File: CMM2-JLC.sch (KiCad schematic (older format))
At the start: 111 parts, among them J1 Nunchuck, J2 VGA, J3 EXTERNAL I/O, J4 USB_C_Receptacle_USB2.0, J5 Audio, J6 USB A Host, J7 SWD, J8 Micro_SD_Card_Det, J9 Boot select, SW1 Reset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

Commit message: Rev B: Hook up SDRAM address line A12
The old sdram symbol did not fit the sdram used. This commit introduces a
new sdram symbol with address line A12 and bumps the revision to Rev B.
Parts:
- U2: symbol Memory_RAM:AS4C4M16SA -> SDRAM_Micron:MT48LC16M16A2
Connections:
- net PG2: now also U2.36 (A12)
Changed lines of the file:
@@
 Title "Colour Maximite 2"
 Date "2020-07-05"
-Rev "A"
+Rev "B"
 Comp "tbspace.de"
 Comment1 "Tobias Mädel"
@@
 $EndDescr
 $Comp
-L Memory_RAM:AS4C4M16SA U2
+L SDRAM_Micron:MT48LC16M16A2 U2
 U 1 1 5F01B402
 P 6600 9300
@@
 Text Label 5600 9350 0    50   ~ 0
 PG1
-Text Label 5600 9600 0    50   ~ 0
+Text Label 5600 9700 0    50   ~ 0
 PG5
-Text Label 5600 9500 0    50   ~ 0
+Text Label 5600 9600 0    50   ~ 0
 PG4
-Text Label 5600 9750 0    50   ~ 0
-PG8
 Text Label 5600 9850 0    50   ~ 0
+PG8
+Text Label 5600 9950 0    50   ~ 0
 PH7
-Text Label 5600 10000 0    50   ~ 0
+Text Label 5600 10050 0    50   ~ 0
 PF11
-Text Label 5600 10100 0    50   ~ 0
+Text Label 5600 10150 0    50   ~ 0
 PG15
-Text Label 5600 10200 0    50   ~ 0
+Text Label 5600 10250 0    50   ~ 0
 PH5
 Text Label 5600 10350 0    50   ~ 0
@@
 	5800 9350 5600 9350
 Wire Wire Line
-	5600 9600 5800 9600
+	5600 9700 5800 9700
 Wire Wire Line
-	5800 9500 5600 9500
+	5800 9600 5600 9600
 Wire Wire Line
-	5600 9750 5800 9750
+	5600 9850 5800 9850
 Wire Wire Line
-	5800 9850 5600 9850
+	5800 9950 5600 9950
 Wire Wire Line
-	5600 10000 5800 10000
+	5600 10050 5800 10050
 Wire Wire Line
-	5800 10100 5600 10100
+	5800 10150 5600 10150
 Wire Wire Line
-	5800 10200 5600 10200
+	5800 10250 5600 10250
 Wire Wire Line
 	5600 10350 5800 10350
@@
 	11050 8500 11500 8500
 Connection ~ 11050 8500
+Text Label 5600 9450 0    50   ~ 0
+PG2
+Wire Wire Line
+	5800 9450 5600 9450
 $EndSCHEMATC

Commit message: Rev C
Some (mostly cosmetic) changes from the final Rev A gerbers were lost in
Rev B due to a corrupted .kicad_pcb file.

This revision reintroduces those changes and improves overall attachment
of groundplanes and islands to one another. Additionally the VGA connector
footprint has been updated to fit the LCSC connector better.

Changelog:
* Restore changes from Rev A gerbers
* Improve grounding
* Update VGA connector footprint for better fit
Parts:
- J2: footprint Connector_Dsub:DSUB-15-HD_Female_Horizontal_P2.29x1.98mm_EdgePinOffset8.35mm_Housed_MountingHolesOffset10.89mm -> CMM2-JLC:DSUB-15-HD_Female_Horizontal_P2.29x2,54mm_EdgePinOffset8.63mm_Housed_MountingHolesOffset11.17mm; symbol Connector:DB15_Female_HighDensity -> Connector:DB15_Female_HighDensity_MountingHoles
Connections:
- net GND: now also J2.0
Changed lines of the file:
@@
 Title "Colour Maximite 2"
 Date "2020-07-05"
-Rev "B"
+Rev "C"
 Comp "tbspace.de"
 Comment1 "Tobias Mädel"
@@
 	1750 5350 1500 5350
 $Comp
-L Connector:DB15_Female_HighDensity J2
+L Connector:DB15_Female_HighDensity_MountingHoles J2
 U 1 1 5FFE2E3E
-P 14550 5250
-F 0 "J2" H 14550 6117 50  0000 C CNN
-F 1 "VGA" H 14550 6026 50  0000 C CNN
-F 2 "Connector_Dsub:DSUB-15-HD_Female_Horizontal_P2.29x1.98mm_EdgePinOffset8.35mm_Housed_MountingHolesOffset10.89mm" H 13600 5650 50  0001 C CNN
-F 3 " ~" H 13600 5650 50  0001 C CNN
-	1    14550 5250
+P 14550 5100
+F 0 "J2" H 14550 5967 50  0000 C CNN
+F 1 "VGA" H 14550 5876 50  0000 C CNN
+F 2 "CMM2-JLC:DSUB-15-HD_Female_Horizontal_P2.29x2,54mm_EdgePinOffset8.63mm_Housed_MountingHolesOffset11.17mm" H 13600 5500 50  0001 C CNN
+F 3 " ~" H 13600 5500 50  0001 C CNN
+	1    14550 5100
 	1    0    0    -1
 $EndComp
@@
 Wire Wire Line
 	15550 1150 15100 1150
-Text Label 13800 4850 0    50   ~ 0
+Text Label 13800 4700 0    50   ~ 0
 VGA_RED
-Text Label 13800 5050 0    50   ~ 0
+Text Label 13800 4900 0    50   ~ 0
 VGA_GREEN
-Text Label 13800 5250 0    50   ~ 0
+Text Label 13800 5100 0    50   ~ 0
 VGA_BLUE
 Wire Wire Line
-	14250 4850 13800 4850
+	14250 4700 13800 4700
 Wire Wire Line
-	13800 5050 14250 5050
+	13800 4900 14250 4900
 Wire Wire Line
-	14250 5250 13800 5250
-Text Label 15350 5250 2    50   ~ 0
+	14250 5100 13800 5100
+Text Label 15350 5100 2    50   ~ 0
 VGA_HSYNC
-Text Label 15350 5450 2    50   ~ 0
+Text Label 15350 5300 2    50   ~ 0
 VGA_VSYNC
-Text Label 15700 5250 2    50   ~ 0
+Text Label 15700 5100 2    50   ~ 0
 PI10
-Text Label 15700 5450 2    50   ~ 0
+Text Label 15700 5300 2    50   ~ 0
 PI9
 Wire Wire Line
-	14850 5250 15700 5250
+	14850 5100 15700 5100
 Wire Wire Line
-	14850 5450 15700 5450
-NoConn ~ 14850 4850
-NoConn ~ 14850 5050
-NoConn ~ 14850 5650
-NoConn ~ 14250 5450
-NoConn ~ 14250 5350
+	14850 5300 15700 5300
+NoConn ~ 14850 4700
+NoConn ~ 14850 4900
+NoConn ~ 14850 5500
+NoConn ~ 14250 5300
+NoConn ~ 14250 5200
 Wire Wire Line
-	14250 4750 13500 4750
+	14250 4600 13500 4600
 Wire Wire Line
-	14250 4950 13500 4950
+	14250 4800 13500 4800
 Wire Wire Line
-	13500 4750 13500 4950
-Connection ~ 13500 4950
+	13500 4600 13500 4800
+Connection ~ 13500 4800
 Wire Wire Line
-	13500 4950 13500 5150
+	13500 4800 13500 5000
 Wire Wire Line
-	14250 5150 13500 5150
-Connection ~ 13500 5150
+	14250 5000 13500 5000
+Connection ~ 13500 5000
 Wire Wire Line
-	13500 5150 13500 5550
+	13500 5000 13500 5400
 Wire Wire Line
-	14250 5550 13500 5550
-Connection ~ 13500 5550
+	14250 5400 13500 5400
+Connection ~ 13500 5400
 Wire Wire Line
-	13500 5550 13500 5650
+	13500 5400 13500 5500
 Wire Wire Line
-	14250 5650 13500 5650
-Connection ~ 13500 5650
-Wire Wire Line
-	13500 5650 13500 5850
+	14250 5500 13500 5500
+Connection ~ 13500 5500
 $Comp
 L power:GND #PWR0117
@@
 Wire Wire Line
 	5800 9450 5600 9450
+Wire Wire Line
+	14550 5800 13500 5800
+Wire Wire Line
+	13500 5500 13500 5800
+Wire Wire Line
+	13500 5800 13500 5850
+Connection ~ 13500 5800
 $EndSCHEMATC

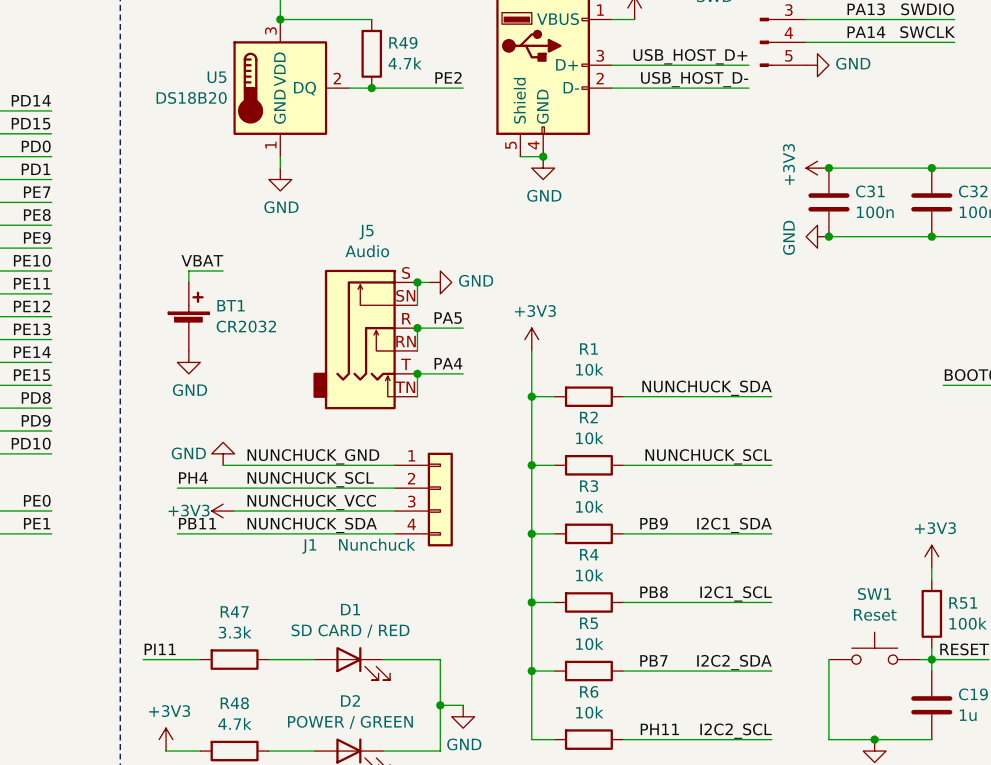
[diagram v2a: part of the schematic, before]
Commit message: Rev D
Changelog:
 * Fix 180° rotated Nunchuk connector
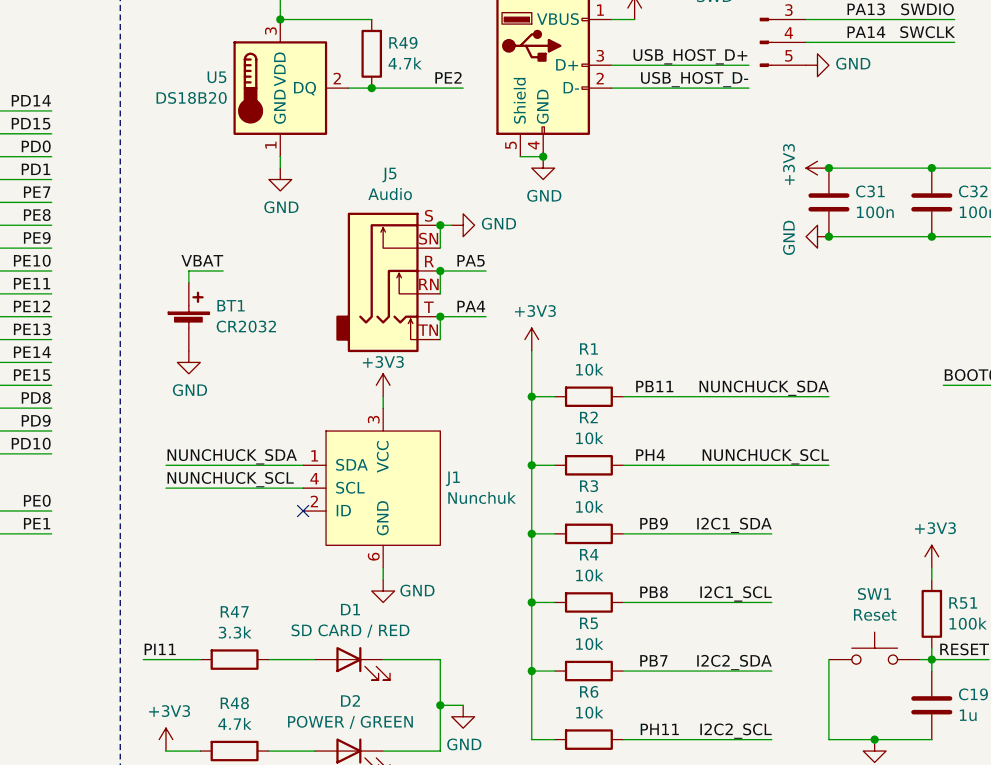
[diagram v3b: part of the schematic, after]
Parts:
- removed J1: Nunchuck, CMM2-JLC:nunchuck, symbol Connector_Generic:Conn_01x04
- added J1: Nunchuk, CMM2-JLC:nunchuck, symbol nunchuk:Nunchuk
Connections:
- net +3V3: now also J1.3 (VCC)
- net GND: now also J1.6 (GND)
- net NUNCHUCK_SCL: now also J1.4 (SCL)
- net NUNCHUCK_SDA: now also J1.1 (SDA)
- no-connect marks 27 -> 28
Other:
- moved on the sheet: J5
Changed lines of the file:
@@
 Title "Colour Maximite 2"
 Date "2020-07-05"
-Rev "C"
+Rev "D"
 Comp "tbspace.de"
 Comment1 "Tobias Mädel"
@@
 	14400 6550 13950 6550
 $Comp
-L Connector_Generic:Conn_01x04 J1
-U 1 1 5F02BAFB
-P 9350 9900
-F 0 "J1" H 8750 9650 50  0000 L CNN
-F 1 "Nunchuck" H 8900 9650 50  0000 L CNN
-F 2 "CMM2-JLC:nunchuck" H 9350 9900 50  0001 C CNN
-F 3 "~" H 9350 9900 50  0001 C CNN
-F 4 "Footprint by Jan Henrik Hemsing -- Thanks! :3" H 9350 9900 50  0001 C CNN "Copyright"
-	1    9350 9900
-	1    0    0    -1
-$EndComp
-Text Label 8500 10000 0    50   ~ 0
-NUNCHUCK_VCC
-Text Label 8500 9800 0    50   ~ 0
-NUNCHUCK_GND
-Text Label 8500 9900 0    50   ~ 0
-NUNCHUCK_SCL
-Text Label 8500 10100 0    50   ~ 0
-NUNCHUCK_SDA
-$Comp
 L power:GND #PWR0107
 U 1 1 5F0C409D
-P 8400 9800
-F 0 "#PWR0107" H 8400 9550 50  0001 C CNN
-F 1 "GND" H 8550 9750 50  0000 C CNN
-F 2 "" H 8400 9800 50  0001 C CNN
-F 3 "" H 8400 9800 50  0001 C CNN
-	1    8400 9800
-	-1   0    0    1
+P 9100 10300
+F 0 "#PWR0107" H 9100 10050 50  0001 C CNN
+F 1 "GND" H 9250 10250 50  0000 C CNN
+F 2 "" H 9100 10300 50  0001 C CNN
+F 3 "" H 9100 10300 50  0001 C CNN
+	1    9100 10300
+	1    0    0    -1
 $EndComp
 $Comp
 L power:+3V3 #PWR0108
 U 1 1 5F0C51CE
-P 8450 10000
-F 0 "#PWR0108" H 8450 9850 50  0001 C CNN
-F 1 "+3V3" V 8450 10200 50  0000 C CNN
-F 2 "" H 8450 10000 50  0001 C CNN
-F 3 "" H 8450 10000 50  0001 C CNN
-	1    8450 10000
-	0    -1   -1   0
+P 9100 9500
+F 0 "#PWR0108" H 9100 9350 50  0001 C CNN
+F 1 "+3V3" H 9100 9650 50  0000 C CNN
+F 2 "" H 9100 9500 50  0001 C CNN
+F 3 "" H 9100 9500 50  0001 C CNN
+	1    9100 9500
+	1    0    0    -1
 $EndComp
-Wire Wire Line
-	8400 9800 9150 9800
-Wire Wire Line
-	8450 10000 9150 10000
 Text Label 4800 4950 2    50   ~ 0
 PB11
-Text Label 10800 9800 2    50   ~ 0
+Text Label 11050 9800 2    50   ~ 0
 NUNCHUCK_SCL
 $Comp
@@
 	0    1    1    0
 $EndComp
-Text Label 10800 9500 2    50   ~ 0
+Text Label 11050 9500 2    50   ~ 0
 NUNCHUCK_SDA
-Wire Wire Line
-	10800 9500 10150 9500
-Wire Wire Line
-	10150 9800 10800 9800
 $Comp
 L Device:R R2
@@
 L Connector:AudioJack3_Switch J5
 U 1 1 60C827BB
-P 9050 9200
-F 0 "J5" H 9032 9625 50  0000 C CNN
-F 1 "Audio" H 9032 9534 50  0000 C CNN
-F 2 "CMM2-JLC:PJ-3270" H 9050 9200 50  0001 C CNN
-F 3 "~" H 9050 9200 50  0001 C CNN
-	1    9050 9200
+P 9150 8950
+F 0 "J5" H 9132 9375 50  0000 C CNN
+F 1 "Audio" H 9132 9284 50  0000 C CNN
+F 2 "CMM2-JLC:PJ-3270" H 9150 8950 50  0001 C CNN
+F 3 "~" H 9150 8950 50  0001 C CNN
+	1    9150 8950
 	1    0    0    -1
 $EndComp
 Wire Wire Line
-	9250 9000 9250 9100
+	9350 8750 9350 8850
 Wire Wire Line
-	9250 9200 9250 9300
+	9350 8950 9350 9050
 Wire Wire Line
-	9250 9400 9250 9500
+	9350 9150 9350 9250
 $Comp
 L power:GND #PWR0123
 U 1 1 60D1AD0A
-P 9300 9000
-F 0 "#PWR0123" H 9300 8750 50  0001 C CNN
-F 1 "GND" V 9305 8872 50  0000 R CNN
-F 2 "" H 9300 9000 50  0001 C CNN
-F 3 "" H 9300 9000 50  0001 C CNN
-	1    9300 9000
+P 9400 8750
+F 0 "#PWR0123" H 9400 8500 50  0001 C CNN
+F 1 "GND" V 9405 8622 50  0000 R CNN
+F 2 "" H 9400 8750 50  0001 C CNN
+F 3 "" H 9400 8750 50  0001 C CNN
+	1    9400 8750
 	0    -1   -1   0
 $EndComp
 Wire Wire Line
-	9250 9000 9300 9000
-Connection ~ 9250 9000
-Text Label 9450 9200 2    50   ~ 0
+	9350 8750 9400 8750
+Connection ~ 9350 8750
+Text Label 9550 8950 2    50   ~ 0
 PA5
-Text Label 9450 9400 2    50   ~ 0
+Text Label 9550 9150 2    50   ~ 0
 PA4
 Wire Wire Line
-	9250 9200 9450 9200
-Connection ~ 9250 9200
+	9350 8950 9550 8950
+Connection ~ 9350 8950
 Wire Wire Line
-	9450 9400 9250 9400
-Connection ~ 9250 9400
+	9550 9150 9350 9150
+Connection ~ 9350 9150
 $Comp
 L Device:LED D1
@@
 Text Label 1500 5950 0    50   ~ 0
 PH4
-Text Label 8200 9900 0    50   ~ 0
-PH4
-Wire Wire Line
-	8200 9900 9150 9900
 Wire Wire Line
 	1500 5950 1750 5950
 Wire Wire Line
 	4800 4950 4550 4950
-Text Label 8200 10100 0    50   ~ 0
+Text Label 10200 9500 0    50   ~ 0
 PB11
-Wire Wire Line
-	8200 10100 9150 10100
 $Comp
 L Switch:SW_Push SW1
@@
 	13500 5800 13500 5850
 Connection ~ 13500 5800
+$Comp
+L nunchuk:Nunchuk J1
+U 1 1 5F5228DA
+P 9100 9900
+F 0 "J1" H 9378 9946 50  0000 L CNN
+F 1 "Nunchuk" H 9378 9855 50  0000 L CNN
+F 2 "CMM2-JLC:nunchuck" H 9100 10400 50  0001 C CNN
+F 3 "" H 9100 10400 50  0001 C CNN
+	1    9100 9900
+	1    0    0    -1
+$EndComp
+Wire Wire Line
+	9100 10300 9100 10250
+Wire Wire Line
+	9100 9500 9100 9550
+NoConn ~ 8750 10000
+Wire Wire Line
+	10150 9500 11050 9500
+Wire Wire Line
+	10150 9800 11050 9800
+Text Label 10200 9800 0    50   ~ 0
+PH4
+Text Label 8150 9800 0    50   ~ 0
+NUNCHUCK_SDA
+Wire Wire Line
+	8150 9800 8750 9800
+Text Label 8150 9900 0    50   ~ 0
+NUNCHUCK_SCL
+Wire Wire Line
+	8150 9900 8750 9900
 $EndSCHEMATC
